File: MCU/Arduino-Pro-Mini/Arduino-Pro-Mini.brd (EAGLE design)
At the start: 17.8 x 33 mm, 19 parts, among them Q1 8/16/20MHz, U1 ATMEGA328

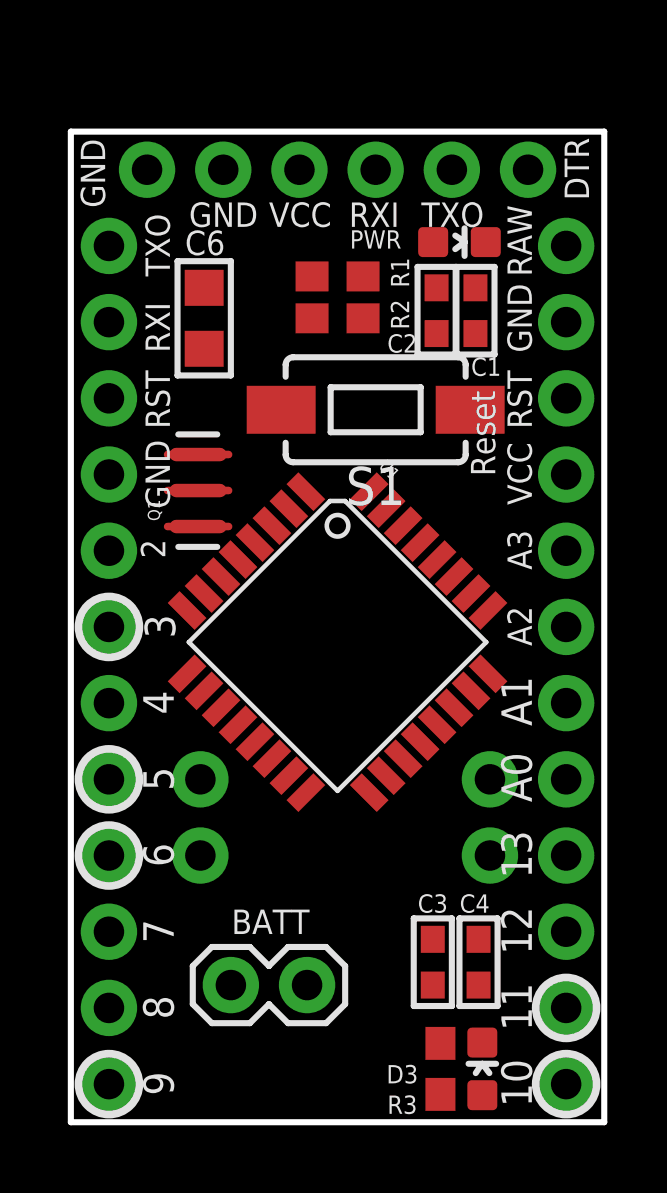
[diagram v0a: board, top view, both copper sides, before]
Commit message: pro mini board route
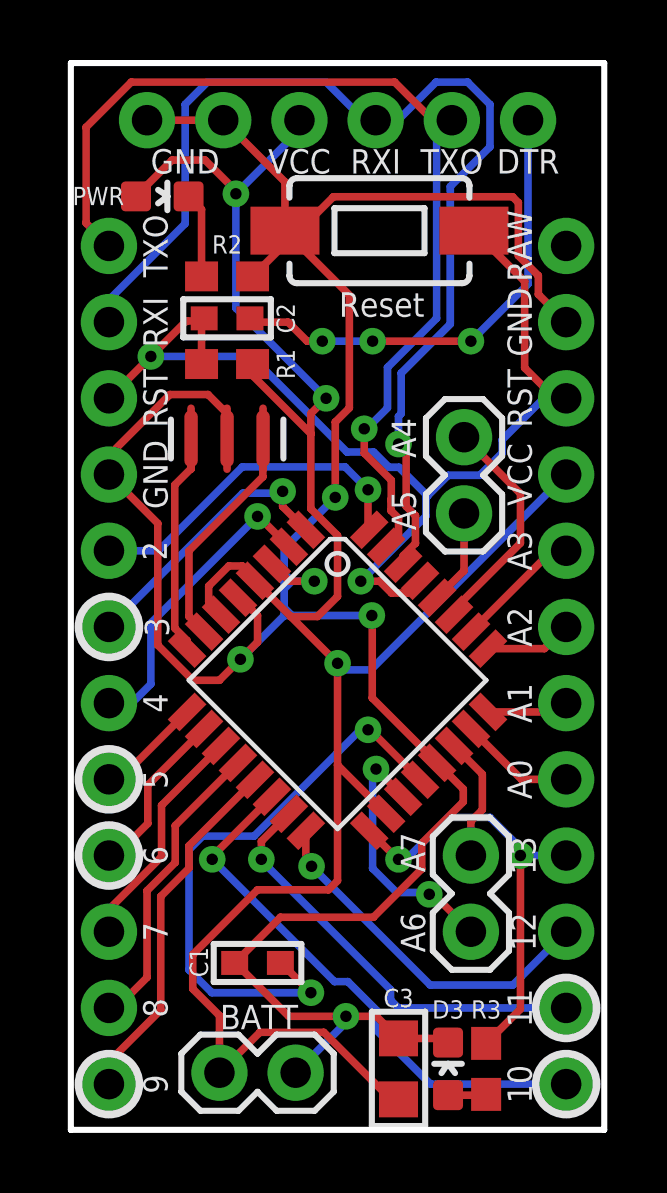
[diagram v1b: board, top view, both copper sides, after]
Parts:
- removed C4: 0.1uF, Scott-Electrical:CAP_0603
- removed C6: 10uF, Scott-Electrical:CAP_0805
- C3: value 0.1uF -> 10uF; device Scott-Electrical:CAP_0603 -> Scott-Electrical:CAP_0805
- moved C1 22.9 mm to (6.22, 5.31), turned to 0 degrees
- moved JP2 14.4 mm to (13.1, 22.8), flipped to the top
- moved PWR 10.0 mm to (3.05, 30.9)
- moved C2 6.99 mm to (5.21, 26.8), turned to 0 degrees
- moved S1 5.97 mm to (10.3, 29.7), turned to 0 degrees
- moved R1 4.70 mm to (5.21, 25.3)
- moved R2 3.94 mm to (5.21, 28.2), turned to 180 degrees
- moved C3 3.74 mm to (10.9, 1.78), turned to 90 degrees
- moved BATT 2.95 mm to (4.95, 1.65)
- moved JP3 2.62 mm to (13.3, 6.35), flipped to the top
- moved Q1 1.98 mm to (5.21, 22.8), turned to 180 degrees
- moved JP1 1.65 mm to (15.2, 33.4)
- moved R3 1.52 mm to (13.8, 1.78)
- moved U1 1.27 mm to (8.89, 14.7)
- moved D3 1.14 mm to (12.6, 1.78)
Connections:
- removed net 3.3V: BATT.1
- net GND: now also C3.2; no longer C3.1, C4.2, C6.2
- net VCC: now also BATT.1, C3.1; no longer C3.2, C4.1, C6.1
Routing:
- net GND: track 0.00 -> 93.1 mm, vias 0 -> 5
- net VCC: track 0.00 -> 72.5 mm, vias 0 -> 3
- net RXI: track 0.00 -> 37.1 mm, vias 0 -> 1
- net RESET: track 0.00 -> 36.2 mm, vias 0 -> 2
- net TXO: track 0.00 -> 33.7 mm, vias 0 -> 1
- net AREF: track 0.00 -> 19.9 mm, vias 0 -> 2
- net D10: track 0.00 -> 18.2 mm, vias 0 -> 1
- net DTR: track 0.00 -> 15.8 mm, vias 0 -> 3
- net SCK: track 0.00 -> 14.9 mm, vias 0 -> 2
- net MOSI: track 0.00 -> 14.3 mm, vias 0 -> 1
- net D9: track 0.00 -> 12.2 mm
- net MISO: track 0.00 -> 12.1 mm, vias 0 -> 1
- net D2: track 0.00 -> 11.5 mm, vias 0 -> 1
- net D4: track 0.00 -> 10.2 mm, vias 0 -> 1
- net D8: track 0.00 -> 10.1 mm
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- removed copper zone on layer 1, net GND
- removed copper zone on layer 16, net GND
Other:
- board size 17.8 x 33 mm -> 17.8 x 35.6 mm
